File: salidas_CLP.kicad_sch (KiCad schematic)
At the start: 28 parts

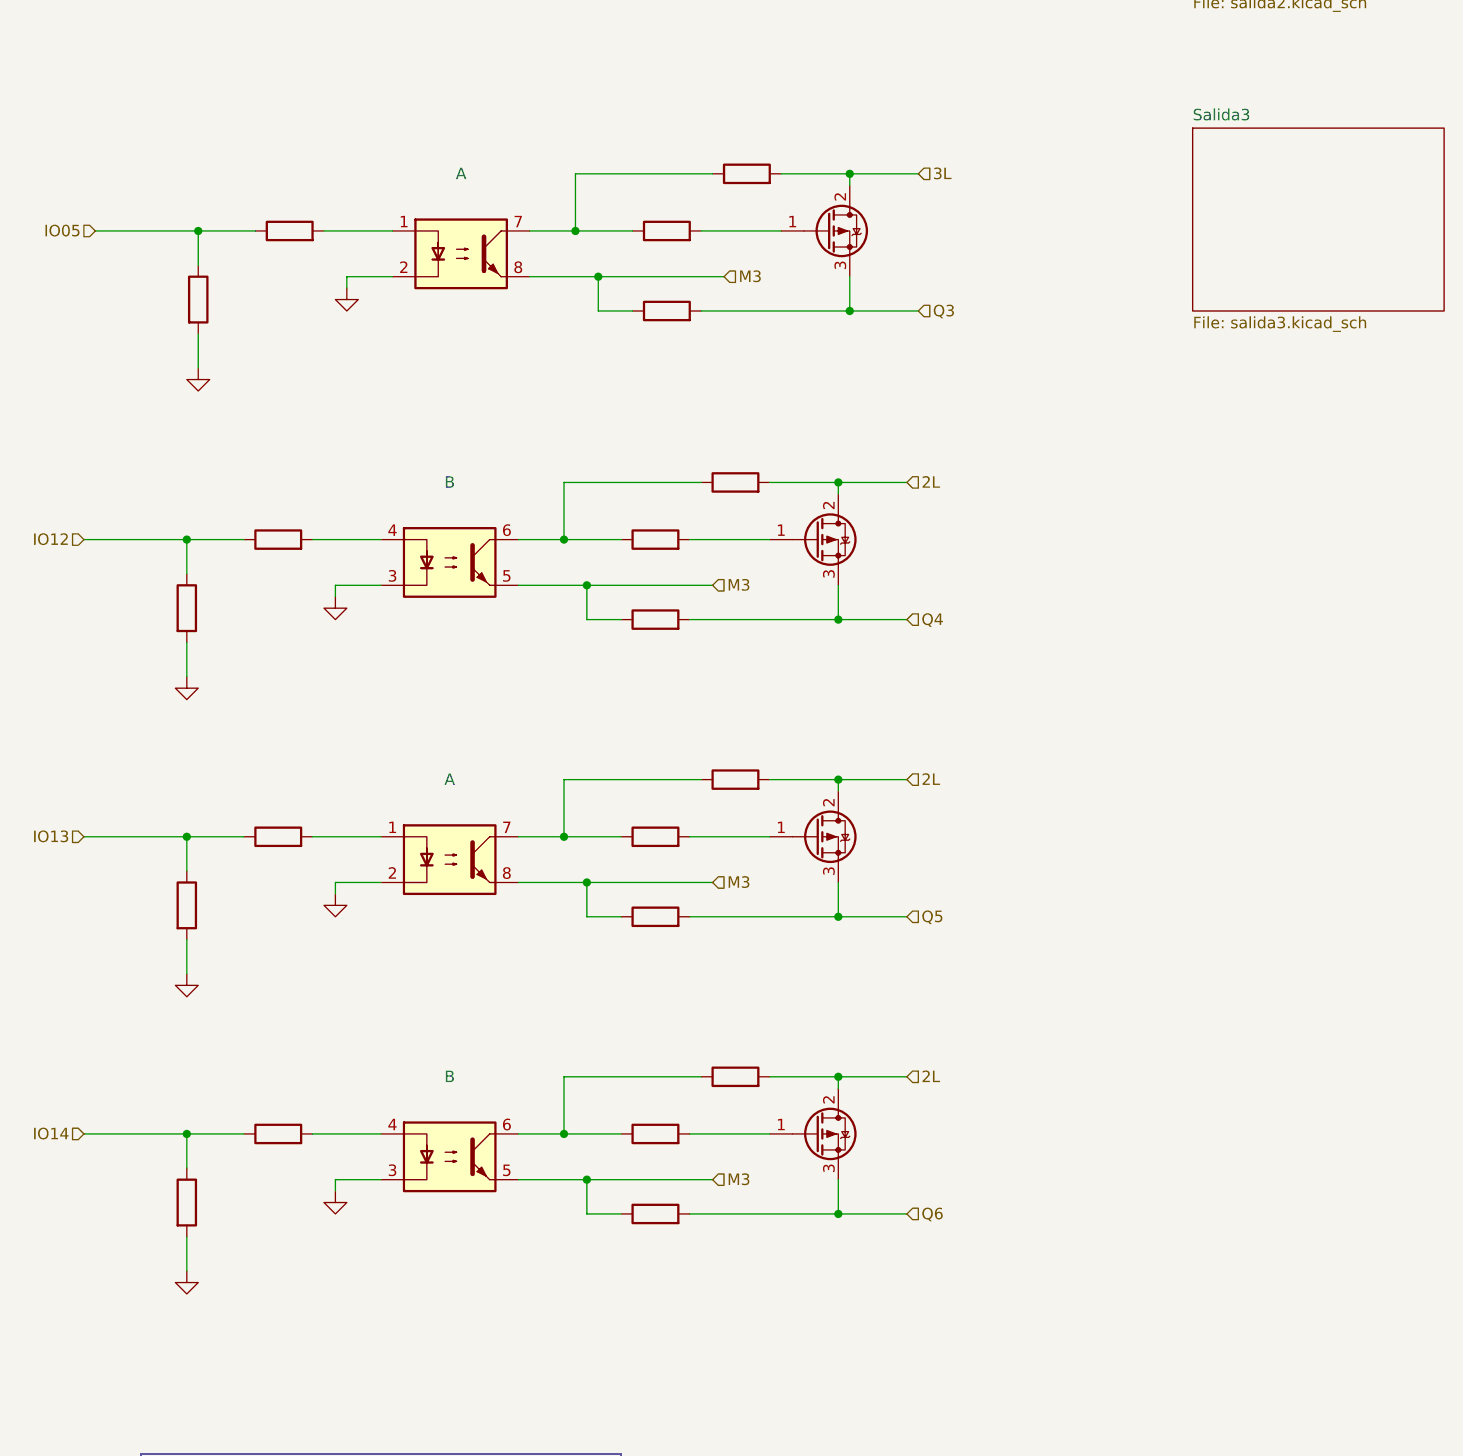
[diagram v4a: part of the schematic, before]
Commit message: add salidas separadas 4,5,6
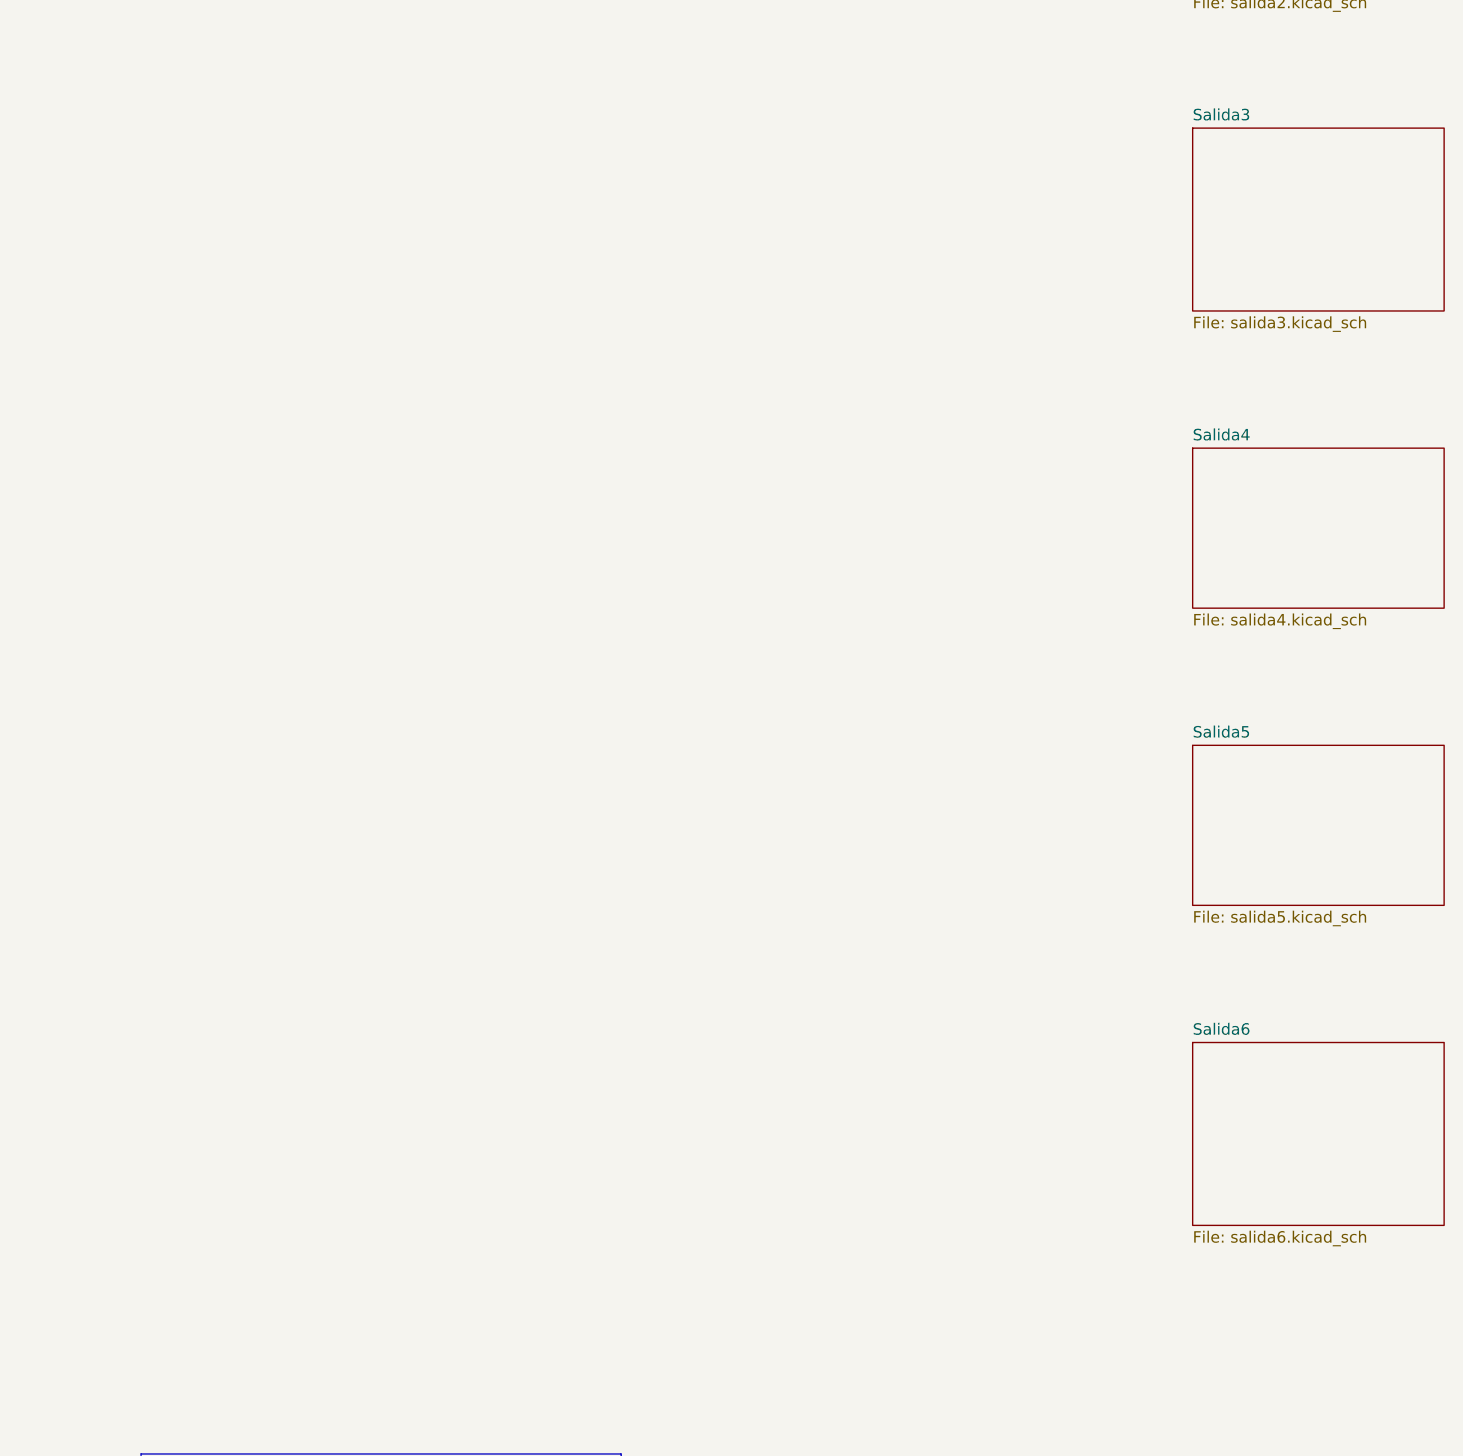
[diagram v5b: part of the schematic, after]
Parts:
- removed ? (x20): (no value), symbol Device:R
- removed ? (x4): (no value), symbol Isolator:ILD74
- removed ? (x4): (no value), symbol Transistor_FET:FQP27P06
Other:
- added sheet Salida4 (salida4.kicad_sch)
- added sheet Salida5 (salida5.kicad_sch)
- added sheet Salida6 (salida6.kicad_sch)

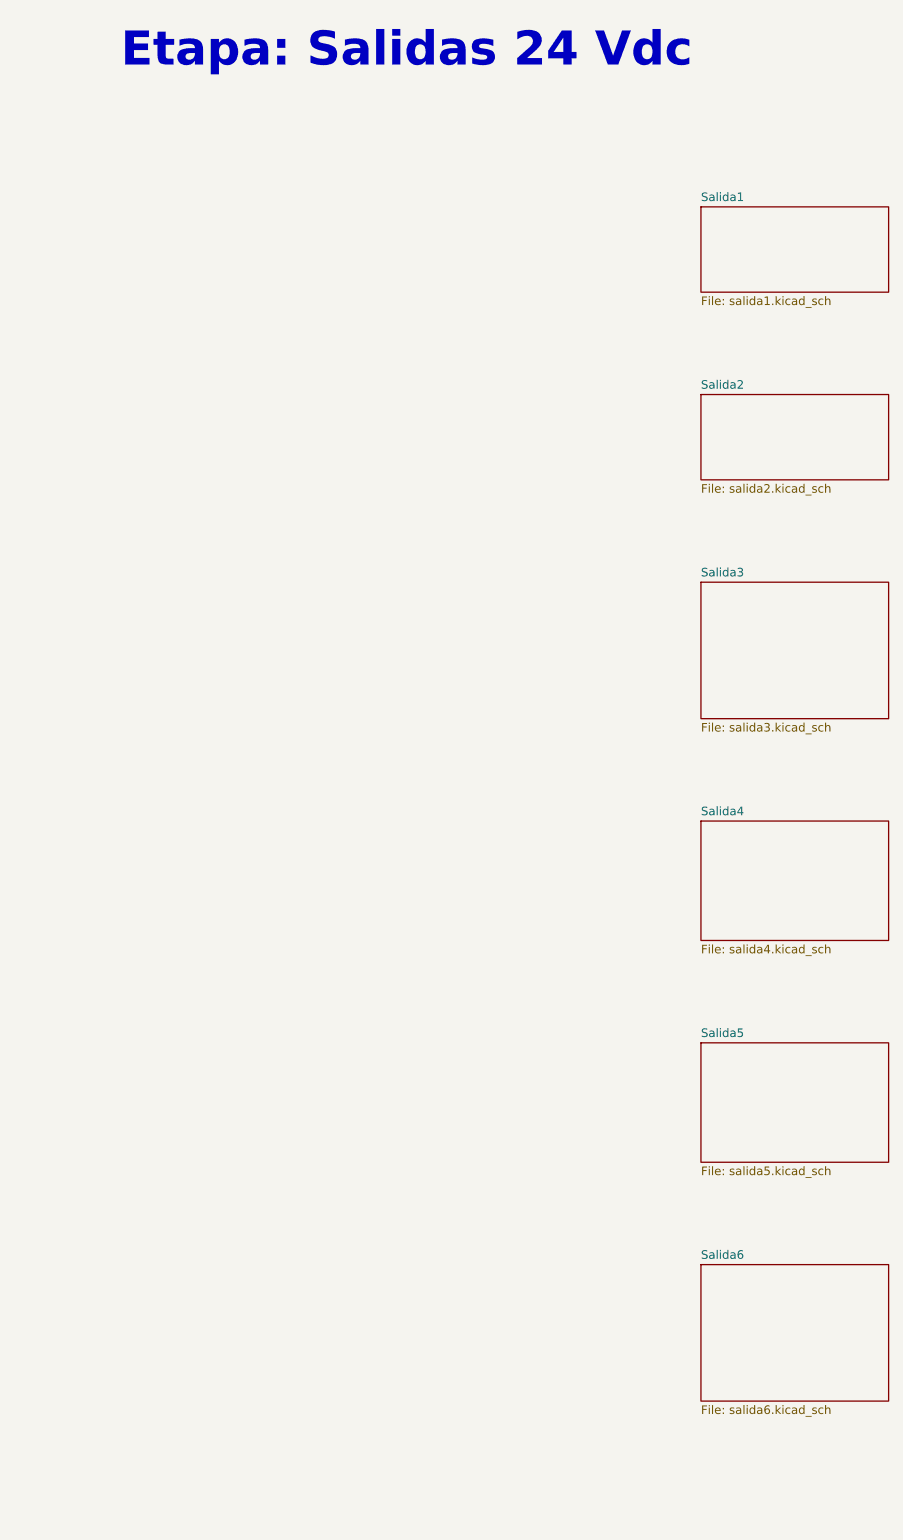
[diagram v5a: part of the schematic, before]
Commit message: add entradas separadas
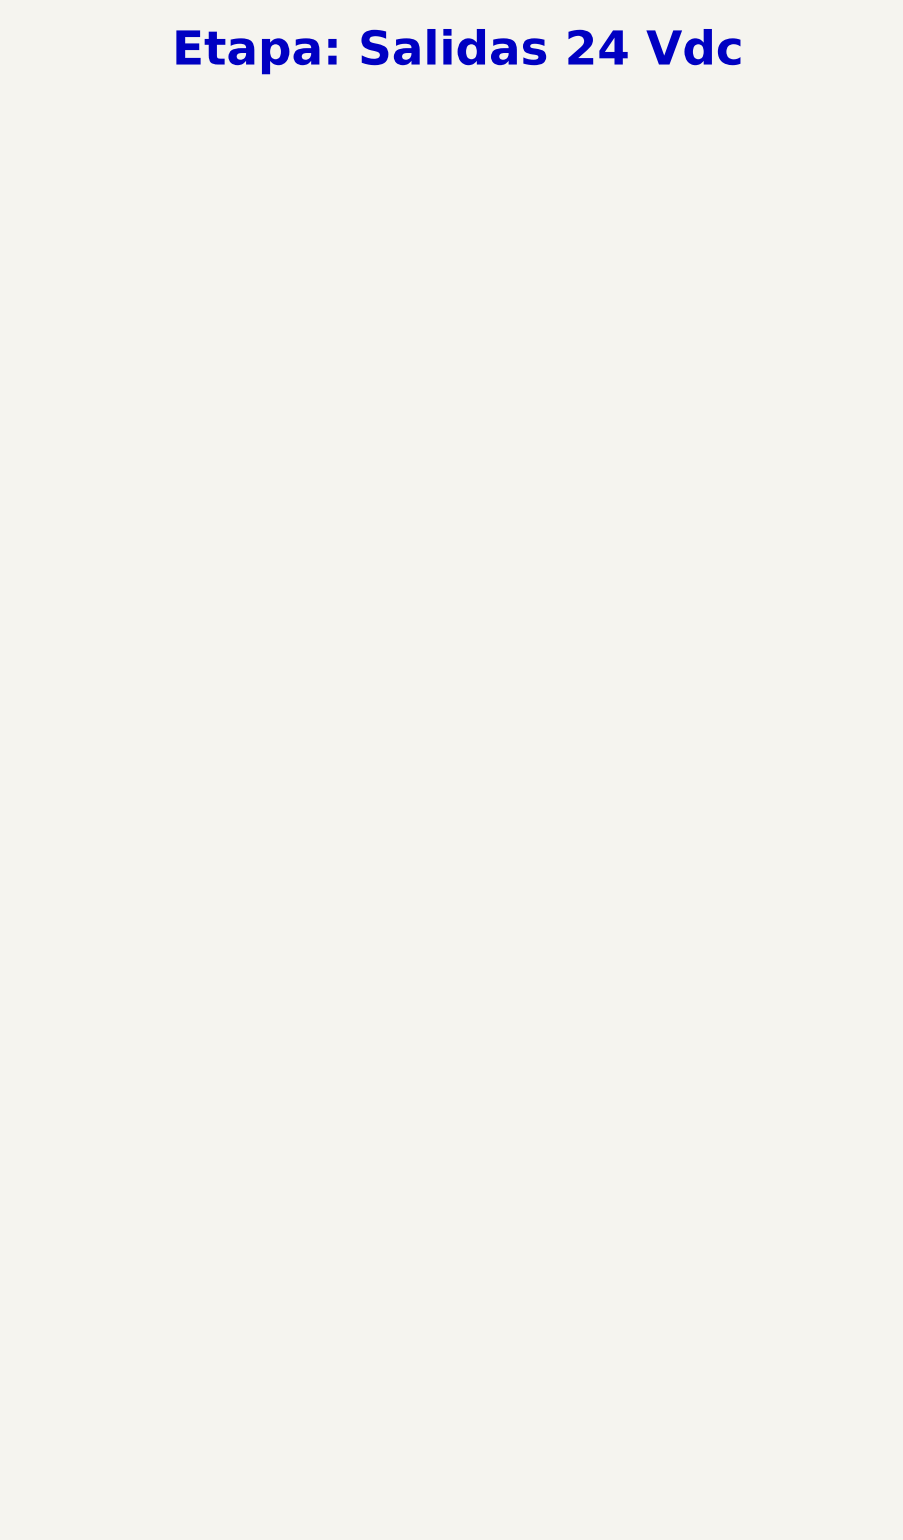
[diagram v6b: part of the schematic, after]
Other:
- removed sheet Salida1
- removed sheet Salida2
- removed sheet Salida3
- removed sheet Salida4
- removed sheet Salida5
- removed sheet Salida6
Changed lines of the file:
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@@
     (stroke (width 0) (type solid) (color 8 0 0 1))
   )
-  (text "Etapa: Salidas 24 Vdc" (at 55.88 30.48 0)
+  (text "Etapa: Salidas 24 Vdc" (at 63.5 30.48 0)
     (effects (font (size 5.08 5.08) (thickness 1.016) bold) (justify left bottom))
   )
@@
     (effects (font (size 2.54 2.54)) (justify left bottom))
   )
-  (sheet (at 142.24 50.8) (size 27.94 12.7) (fields_autoplaced)
-    (stroke (width 0.1524) (type solid))
-    (fill (color 0 0 0 0.0000))
-    (property "Sheetname" "Salida1" (at 142.24 50.0884 0)
-      (effects (font (size 1.27 1.27)) (justify left bottom))
-    )
-    (property "Sheetfile" "salida1.kicad_sch" (at 142.24 64.0846 0)
-      (effects (font (size 1.27 1.27)) (justify left top))
-    )
-  )
-  (sheet (at 142.24 142.24) (size 27.94 17.78) (fields_autoplaced)
-    (stroke (width 0.1524) (type solid))
-    (fill (color 0 0 0 0.0000))
-    (property "Sheetname" "Salida4" (at 142.24 141.5284 0)
-      (effects (font (size 1.27 1.27)) (justify left bottom))
-    )
-    (property "Sheetfile" "salida4.kicad_sch" (at 142.24 160.6046 0)
-      (effects (font (size 1.27 1.27)) (justify left top))
-    )
-  )
-  (sheet (at 142.24 208.28) (size 27.94 20.32) (fields_autoplaced)
-    (stroke (width 0.1524) (type solid))
-    (fill (color 0 0 0 0.0000))
-    (property "Sheetname" "Salida6" (at 142.24 207.5684 0)
-      (effects (font (size 1.27 1.27)) (justify left bottom))
-    )
-    (property "Sheetfile" "salida6.kicad_sch" (at 142.24 229.1846 0)
-      (effects (font (size 1.27 1.27)) (justify left top))
-    )
-  )
-  (sheet (at 142.24 175.26) (size 27.94 17.78) (fields_autoplaced)
-    (stroke (width 0.1524) (type solid))
-    (fill (color 0 0 0 0.0000))
-    (property "Sheetname" "Salida5" (at 142.24 174.5484 0)
-      (effects (font (size 1.27 1.27)) (justify left bottom))
-    )
-    (property "Sheetfile" "salida5.kicad_sch" (at 142.24 193.6246 0)
-      (effects (font (size 1.27 1.27)) (justify left top))
-    )
-  )
-  (sheet (at 142.24 106.68) (size 27.94 20.32) (fields_autoplaced)
-    (stroke (width 0.1524) (type solid))
-    (fill (color 0 0 0 0.0000))
-    (property "Sheetname" "Salida3" (at 142.24 105.9684 0)
-      (effects (font (size 1.27 1.27)) (justify left bottom))
-    )
-    (property "Sheetfile" "salida3.kicad_sch" (at 142.24 127.5846 0)
-      (effects (font (size 1.27 1.27)) (justify left top))
-    )
-  )
-  (sheet (at 142.24 78.74) (size 27.94 12.7) (fields_autoplaced)
-    (stroke (width 0.1524) (type solid))
-    (fill (color 0 0 0 0.0000))
-    (property "Sheetname" "Salida2" (at 142.24 78.0284 0)
-      (effects (font (size 1.27 1.27)) (justify left bottom))
-    )
-    (property "Sheetfile" "salida2.kicad_sch" (at 142.24 92.0246 0)
-      (effects (font (size 1.27 1.27)) (justify left top))
-    )
-  )
 )
